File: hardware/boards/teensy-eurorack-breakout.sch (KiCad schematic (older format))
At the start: 74 parts, among them J1 Conn_01x08, SW1 Rotary_Encoder_Switch, SW2 Rotary_Encoder_Switch, SW3 Rotary_Encoder_Switch, U2 AD5754BREZ, U3 AD5754BREZ, U5 MCP1700-2502E, U6 AD7606BSTZ, U7 6N138

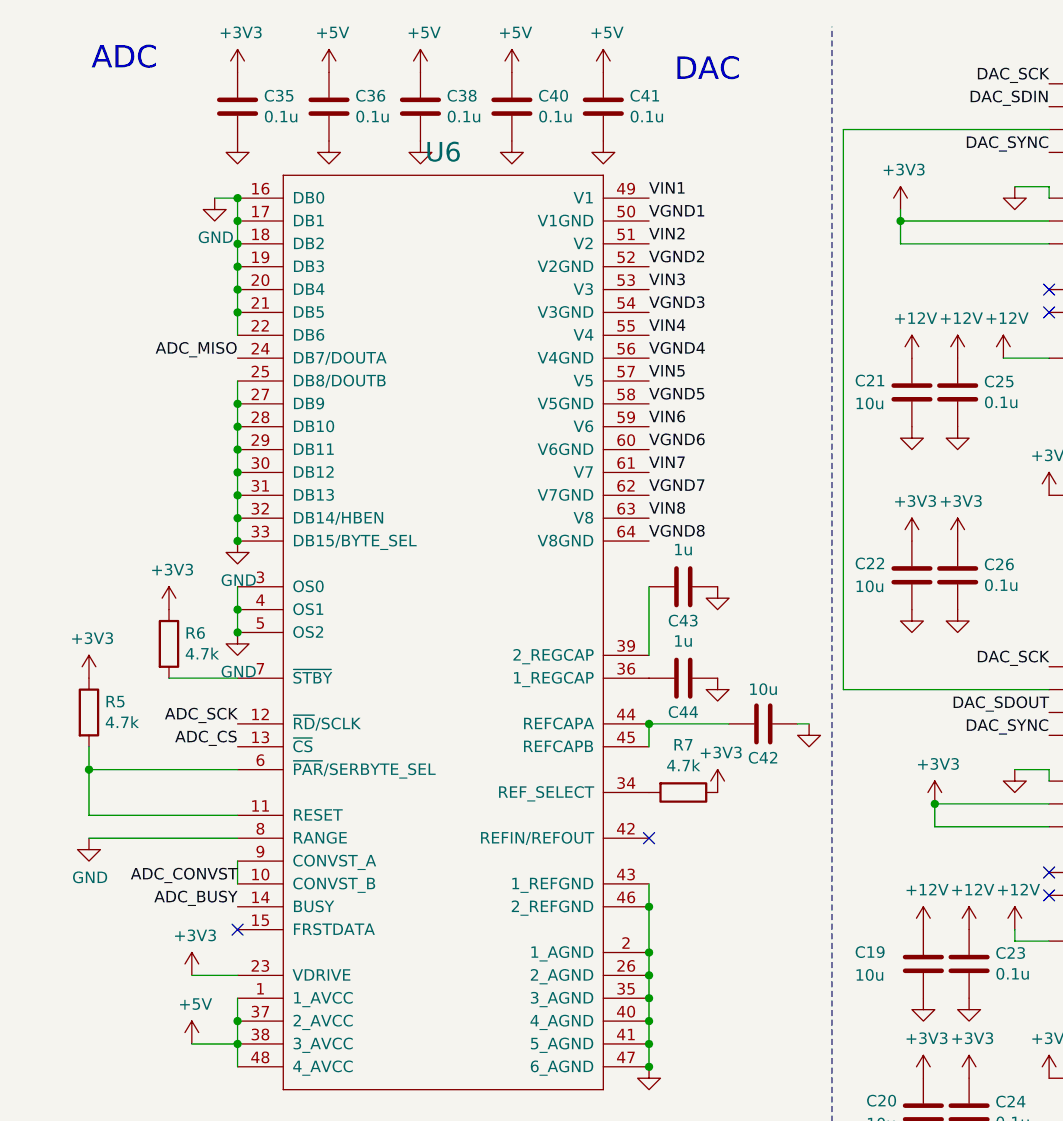
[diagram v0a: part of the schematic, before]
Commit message: fix schematic errors and change breakout to 4 layer board
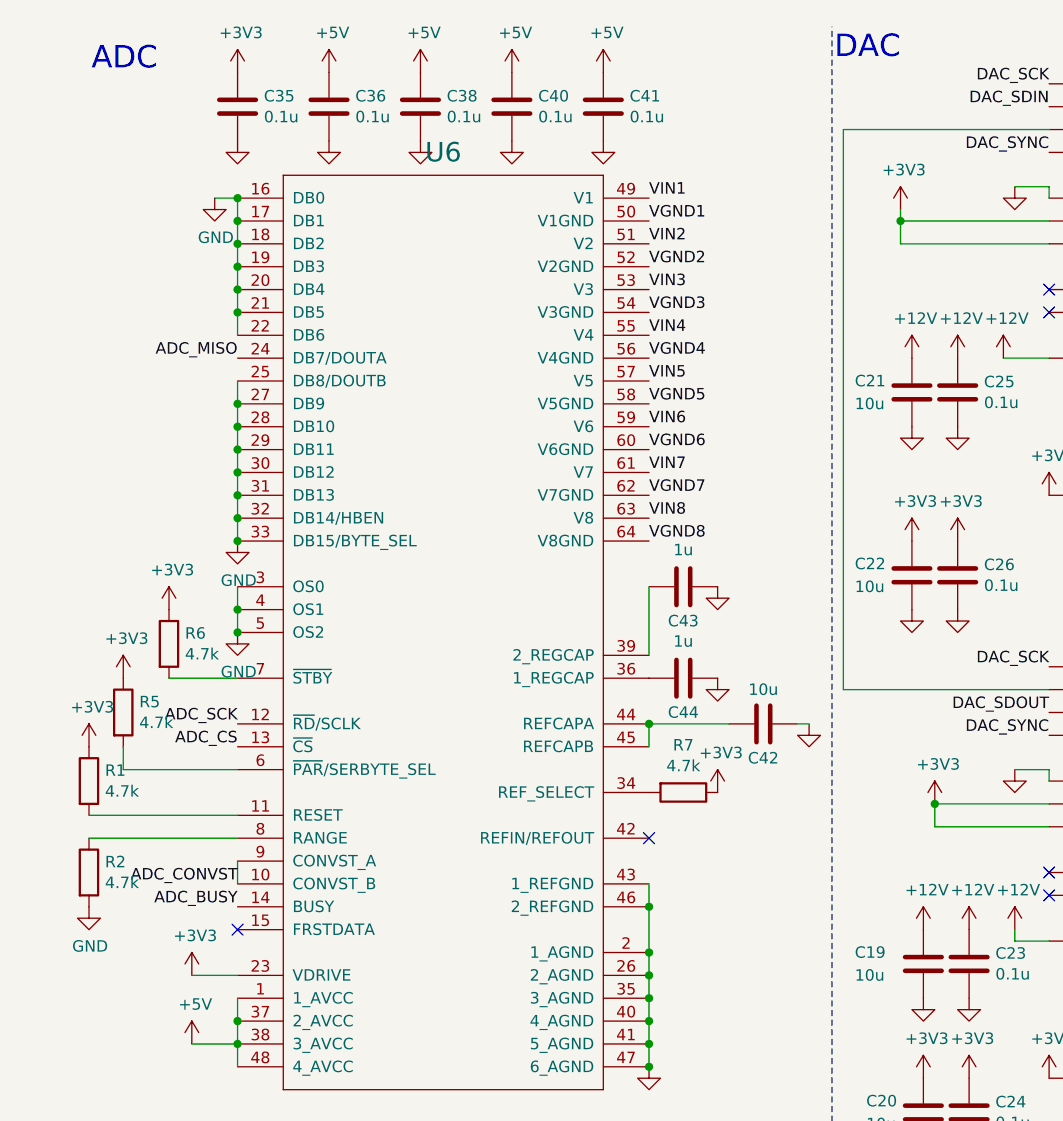
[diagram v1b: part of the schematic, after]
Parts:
- added R1, R2: 4.7k, Resistor_SMD:R_0805_2012Metric, symbol Device:R
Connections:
- net +3V3: now also R1.1
- net GND: now also R2.2; no longer U6.8 (RANGE)
- net at R5.2, U6.6 (~PAR~/SERBYTE_SEL): no longer U6.11 (RESET)
- new net: R1.2, U6.11 (RESET)
- new net: R2.1, U6.8 (RANGE)
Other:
- moved on the sheet: R5
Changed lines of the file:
@@
 L Device:R R5
 U 1 1 5EE69443
-P 550 3500
-F 0 "R5" H 620 3546 50  0000 L CNN
-F 1 "4.7k" H 620 3455 50  0000 L CNN
-F 2 "Resistor_SMD:R_0805_2012Metric" V 480 3500 50  0001 C CNN
-F 3 "~" H 550 3500 50  0001 C CNN
-	1    550  3500
-	1    0    0    -1
-$EndComp
-Wire Wire Line
-	550  3650 550  3750
-Wire Wire Line
-	550  3750 1200 3750
+P 700 3500
+F 0 "R5" H 770 3546 50  0000 L CNN
+F 1 "4.7k" H 770 3455 50  0000 L CNN
+F 2 "Resistor_SMD:R_0805_2012Metric" V 630 3500 50  0001 C CNN
+F 3 "~" H 700 3500 50  0001 C CNN
+	1    700  3500
+	1    0    0    -1
+$EndComp
 $Comp
 L power:+3V3 #PWR073
 U 1 1 5EE6BD54
-P 550 3350
-F 0 "#PWR073" H 550 3200 50  0001 C CNN
-F 1 "+3V3" H 565 3523 50  0000 C CNN
-F 2 "" H 550 3350 50  0001 C CNN
-F 3 "" H 550 3350 50  0001 C CNN
-	1    550  3350
+P 700 3350
+F 0 "#PWR073" H 700 3200 50  0001 C CNN
+F 1 "+3V3" H 715 3523 50  0000 C CNN
+F 2 "" H 700 3350 50  0001 C CNN
+F 3 "" H 700 3350 50  0001 C CNN
+	1    700  3350
 	1    0    0    -1
 $EndComp
@@
 L power:GND #PWR074
 U 1 1 5EE71FB6
-P 550 4050
-F 0 "#PWR074" H 550 3800 50  0001 C CNN
-F 1 "GND" H 555 3877 50  0000 C CNN
-F 2 "" H 550 4050 50  0001 C CNN
-F 3 "" H 550 4050 50  0001 C CNN
-	1    550  4050
+P 550 4350
+F 0 "#PWR074" H 550 4100 50  0001 C CNN
+F 1 "GND" H 555 4177 50  0000 C CNN
+F 2 "" H 550 4350 50  0001 C CNN
+F 3 "" H 550 4350 50  0001 C CNN
+	1    550  4350
 	1    0    0    -1
 $EndComp
@@
 	7950 9550 8000 9550
 Wire Wire Line
-	550  3750 550  3950
-Wire Wire Line
 	550  3950 1200 3950
-Connection ~ 550  3750
 $Comp
 L power:GND #PWR077
@@
 	1    0    0    1
 $EndComp
-Text Notes 3400 750  2    98   ~ 0
+Text Notes 4100 650  2    98   ~ 0
 DAC
 Text Label 6150 3800 0    50   ~ 0
@@
 Wire Notes Line
 	500  5550 7000 5550
+Wire Wire Line
+	700  3650 700  3750
+Wire Wire Line
+	700  3750 1200 3750
+$Comp
+L Device:R R1
+U 1 1 5F517C04
+P 550 3800
+F 0 "R1" H 620 3846 50  0000 L CNN
+F 1 "4.7k" H 620 3755 50  0000 L CNN
+F 2 "Resistor_SMD:R_0805_2012Metric" V 480 3800 50  0001 C CNN
+F 3 "~" H 550 3800 50  0001 C CNN
+	1    550  3800
+	1    0    0    -1
+$EndComp
+$Comp
+L power:+3V3 #PWR01
+U 1 1 5F517C0A
+P 550 3650
+F 0 "#PWR01" H 550 3500 50  0001 C CNN
+F 1 "+3V3" H 565 3823 50  0000 C CNN
+F 2 "" H 550 3650 50  0001 C CNN
+F 3 "" H 550 3650 50  0001 C CNN
+	1    550  3650
+	1    0    0    -1
+$EndComp
+$Comp
+L Device:R R2
+U 1 1 5F5296C2
+P 550 4200
+F 0 "R2" H 620 4246 50  0000 L CNN
+F 1 "4.7k" H 620 4155 50  0000 L CNN
+F 2 "Resistor_SMD:R_0805_2012Metric" V 480 4200 50  0001 C CNN
+F 3 "~" H 550 4200 50  0001 C CNN
+	1    550  4200
+	1    0    0    -1
+$EndComp
 $EndSCHEMATC

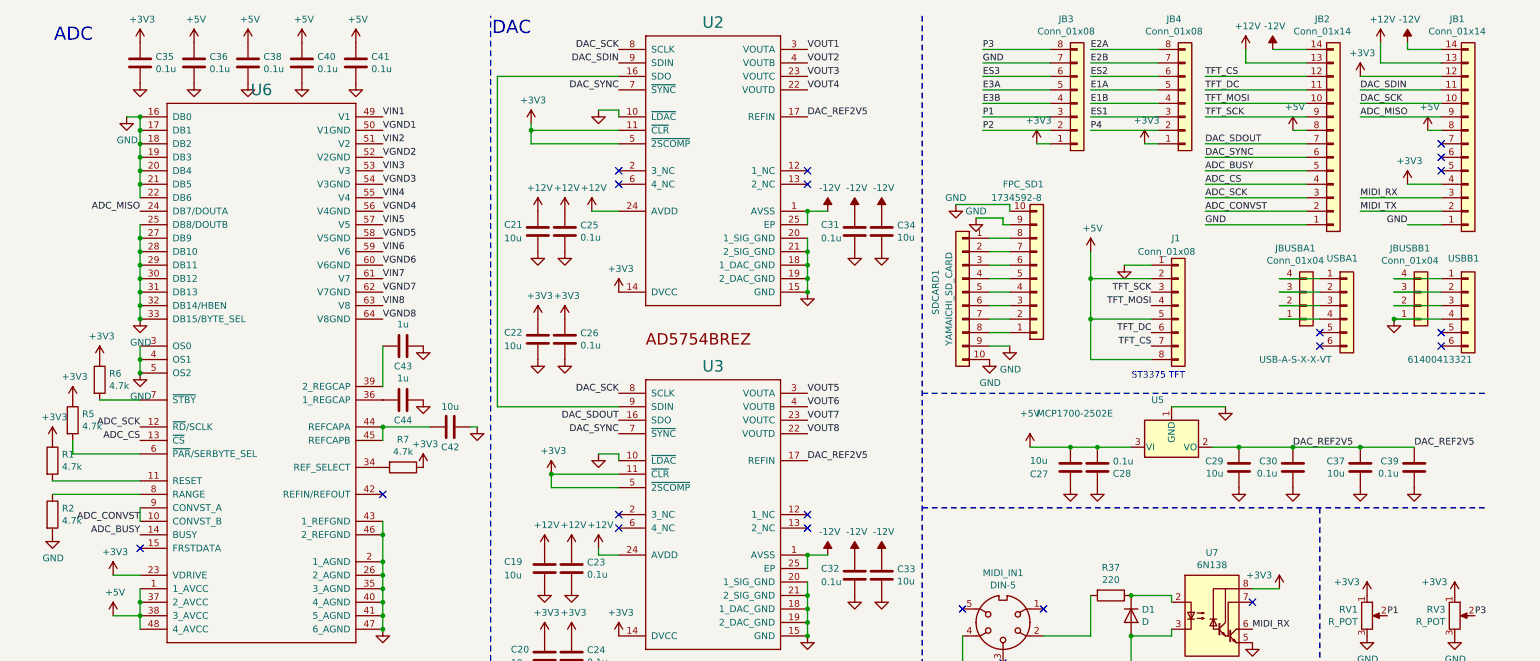
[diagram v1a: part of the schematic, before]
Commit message: schematic: corrections and updates
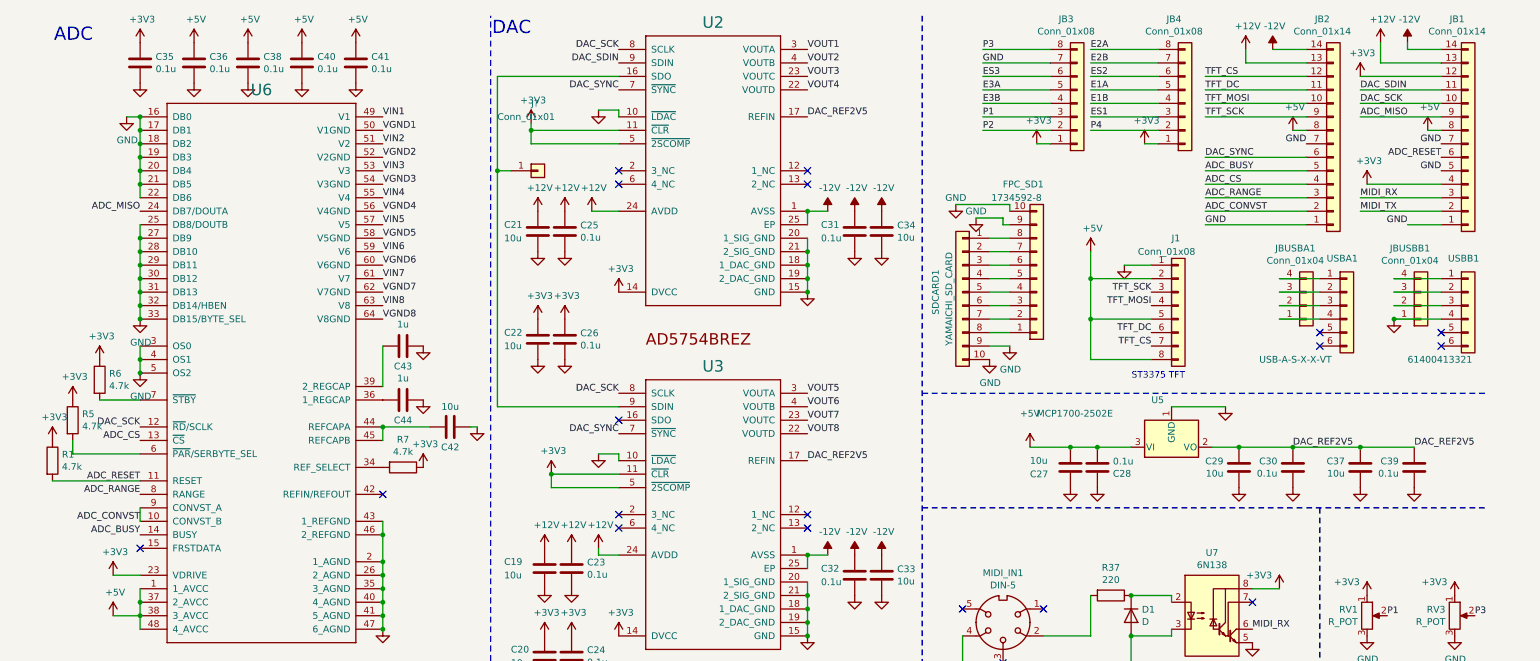
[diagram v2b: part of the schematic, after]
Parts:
- removed R2: 4.7k, Resistor_SMD:R_0805_2012Metric, symbol Device:R
- added J?: Conn_01x01, symbol Connector_Generic:Conn_01x01
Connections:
- net DAC_SCK: now also U6.12 (~RD~/SCLK)
- net GND: now also JB1.5 (Pin_5), JB1.7 (Pin_7), JB2.7 (Pin_7)
- net ADC_RESET: now reaches R1.2, U6.11 (RESET)
- net ADC_RESET: now also JB1.6 (Pin_6)
- net ADC_RANGE: now reaches U6.8 (RANGE)
- net ADC_RANGE: now also JB2.3 (Pin_3)
- net at U2.16 (SDO), U3.9 (SDIN): now also J?.1 (Pin_1)
- removed net ADC_SCK: JB2.3 (Pin_3), U6.12 (~RD~/SCLK)
- net DAC_SDOUT: no longer names the net of U3.16 (SDO)
- net DAC_SDOUT: no longer JB2.7 (Pin_7)
- no-connect marks 32 -> 30
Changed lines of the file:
@@
 Text Label 1200 1950 2    50   ~ 0
 ADC_MISO
-Text Label 1200 3550 2    50   ~ 0
-ADC_SCK
 Text Label 1200 3650 2    50   ~ 0
 ADC_CS
@@
 	1    0    0    -1
 $EndComp
-$Comp
-L power:GND #PWR074
-U 1 1 5EE71FB6
-P 550 4350
-F 0 "#PWR074" H 550 4100 50  0001 C CNN
-F 1 "GND" H 555 4177 50  0000 C CNN
-F 2 "" H 550 4350 50  0001 C CNN
-F 3 "" H 550 4350 50  0001 C CNN
-	1    550  4350
-	1    0    0    -1
-$EndComp
-Wire Wire Line
-	550  4050 1200 4050
 Wire Wire Line
 	1200 4150 1200 4250
@@
 L power:+3V3 #PWR083
 U 1 1 5F063899
-P 10600 1750
-F 0 "#PWR083" H 10600 1600 50  0001 C CNN
-F 1 "+3V3" H 10615 1923 50  0000 C CNN
-F 2 "" H 10600 1750 50  0001 C CNN
-F 3 "" H 10600 1750 50  0001 C CNN
-	1    10600 1750
+P 10300 1750
+F 0 "#PWR083" H 10300 1600 50  0001 C CNN
+F 1 "+3V3" H 10315 1923 50  0000 C CNN
+F 2 "" H 10300 1750 50  0001 C CNN
+F 3 "" H 10300 1750 50  0001 C CNN
+	1    10300 1750
 	1    0    0    -1
 $EndComp
@@
 Text Label 7450 750  0    49   ~ 0
 P3
-$Comp
-L Connector_Generic:Conn_01x14 JB1
-U 1 1 5EF74B39
-P 11050 1450
-F 0 "JB1" H 10968 525 50  0000 C CNN
-F 1 "Conn_01x14" H 10968 616 50  0000 C CNN
-F 2 "Connector_PinSocket_2.54mm:PinSocket_1x14_P2.54mm_Vertical" H 11050 1450 50  0001 C CNN
-F 3 "~" H 11050 1450 50  0001 C CNN
-	1    11050 1450
-	1    0    0    1
-$EndComp
 Wire Wire Line
 	10250 1950 10850 1950
@@
 	-1   0    0    -1
 $EndComp
-NoConn ~ 10850 1450
-NoConn ~ 10850 1550
-NoConn ~ 10850 1650
 NoConn ~ 850  7650
 NoConn ~ 1600 7650
@@
 Wire Wire Line
 	10250 950  10850 950
-Wire Wire Line
-	10600 1750 10850 1750
 Wire Wire Line
 	7850 1450 7950 1450
@@
 	1    0    0    -1
 $EndComp
-Text Label 4750 3500 2    50   ~ 0
-DAC_SDOUT
 NoConn ~ 4750 4300
 NoConn ~ 4750 4200
@@
 	3850 3400 4750 3400
 Wire Wire Line
-	3850 950  3850 3400
+	3850 950  3850 1650
 Wire Wire Line
 	4750 950  3850 950
@@
 	9100 1250 9850 1250
 Wire Wire Line
-	9850 1450 9100 1450
-Wire Wire Line
 	9850 1550 9100 1550
 Text Label 9100 1650 0    49   ~ 0
@@
 ADC_CONVST
 Text Label 9100 1850 0    49   ~ 0
-ADC_SCK
+ADC_RANGE
 Text Label 9100 1750 0    49   ~ 0
 ADC_CS
@@
 Text Label 9100 1550 0    49   ~ 0
 DAC_SYNC
-Text Label 9100 1450 0    49   ~ 0
-DAC_SDOUT
 Wire Wire Line
 	9100 2050 9850 2050
@@
 	1    0    0    -1
 $EndComp
-$Comp
-L Device:R R2
-U 1 1 5F5296C2
-P 550 4200
-F 0 "R2" H 620 4246 50  0000 L CNN
-F 1 "4.7k" H 620 4155 50  0000 L CNN
-F 2 "Resistor_SMD:R_0805_2012Metric" V 480 4200 50  0001 C CNN
-F 3 "~" H 550 4200 50  0001 C CNN
-	1    550  4200
-	1    0    0    -1
-$EndComp
+Text Label 1200 4050 2    49   ~ 0
+ADC_RANGE
+Text Label 1200 3550 2    50   ~ 0
+DAC_SCK
+$Comp
+L Connector_Generic:Conn_01x01 J?
+U 1 1 5FA6E2AB
+P 4150 1650
+F 0 "J?" H 4100 2150 50  0000 L CNN
+F 1 "Conn_01x01" H 3850 2050 50  0000 L CNN
+F 2 "" H 4150 1650 50  0001 C CNN
+F 3 "" H 4150 1650 50  0001 C CNN
+	1    4150 1650
+	1    0    0    -1
+$EndComp
+Wire Wire Line
+	3950 1650 3850 1650
+Connection ~ 3850 1650
+Wire Wire Line
+	3850 1650 3850 3400
+NoConn ~ 4750 3500
+Text Label 9850 1450 2    49   ~ 0
+GND
+$Comp
+L Connector_Generic:Conn_01x14 JB1
+U 1 1 5EF74B39
+P 11050 1450
+F 0 "JB1" H 10968 525 50  0000 C CNN
+F 1 "Conn_01x14" H 10968 616 50  0000 C CNN
+F 2 "Connector_PinSocket_2.54mm:PinSocket_1x14_P2.54mm_Vertical" H 11050 1450 50  0001 C CNN
+F 3 "~" H 11050 1450 50  0001 C CNN
+	1    11050 1450
+	1    0    0    1
+$EndComp
+Text Label 10850 1450 2    49   ~ 0
+GND
+Text Label 10850 1650 2    49   ~ 0
+GND
+Text Label 10850 1550 2    49   ~ 0
+ADC_RESET
+Text Label 1200 3950 2    49   ~ 0
+ADC_RESET
+Wire Wire Line
+	10300 1750 10850 1750
 $EndSCHEMATC

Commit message: schematic, pcb changes for v2.0
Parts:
- removed J?: Conn_01x01, symbol Connector_Generic:Conn_01x01
- C19, C21, C23, C25, C31, C32, C33, C34: footprint Capacitor_SMD:C_0805_2012Metric -> Capacitors_THT:CP_Radial_D5.0mm_P2.00mm
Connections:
- net +12V: now also JB1.14 (Pin_14); no longer JB1.13 (Pin_13), JB2.13 (Pin_13)
- net -12V: now also JB1.13 (Pin_13); no longer JB1.14 (Pin_14), JB2.14 (Pin_14)
- no-connect marks 30 -> 32
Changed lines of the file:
@@
 	10250 1250 10850 1250
-$Comp
-L power:-12V #PWR0150
-U 1 1 5F09F1EE
-P 10600 700
-F 0 "#PWR0150" H 10600 800 50  0001 C CNN
-F 1 "-12V" H 10615 873 50  0000 C CNN
-F 2 "" H 10600 700 50  0001 C CNN
-F 3 "" H 10600 700 50  0001 C CNN
-	1    10600 700
-	1    0    0    -1
-$EndComp
-$Comp
-L power:+12V #PWR0153
-U 1 1 5F0A0CCB
-P 10400 700
-F 0 "#PWR0153" H 10400 550 50  0001 C CNN
-F 1 "+12V" H 10415 873 50  0000 C CNN
-F 2 "" H 10400 700 50  0001 C CNN
-F 3 "" H 10400 700 50  0001 C CNN
-	1    10400 700
-	1    0    0    -1
-$EndComp
-Wire Wire Line
-	10600 700  10600 750
-Wire Wire Line
-	10600 750  10850 750
-Wire Wire Line
-	10400 700  10400 850
-Wire Wire Line
-	10400 850  10850 850
 $Comp
 L power:+5V #PWR0154
@@
 F 0 "C33" H 6815 4696 50  0000 L CNN
 F 1 "10u" H 6815 4605 50  0000 L CNN
-F 2 "Capacitor_SMD:C_0805_2012Metric" H 6738 4500 50  0001 C CNN
+F 2 "Capacitors_THT:CP_Radial_D5.0mm_P2.00mm" H 6738 4500 50  0001 C CNN
 F 3 "~" H 6700 4650 50  0001 C CNN
 	1    6700 4650
@@
 F 0 "C32" H 6250 4700 50  0000 L CNN
 F 1 "0.1u" H 6250 4600 50  0000 L CNN
-F 2 "Capacitor_SMD:C_0805_2012Metric" H 6538 4500 50  0001 C CNN
+F 2 "Capacitors_THT:CP_Radial_D5.0mm_P2.00mm" H 6538 4500 50  0001 C CNN
 F 3 "~" H 6500 4650 50  0001 C CNN
 	1    6500 4650
@@
 F 0 "C23" H 4515 4646 50  0000 L CNN
 F 1 "0.1u" H 4515 4555 50  0000 L CNN
-F 2 "Capacitor_SMD:C_0805_2012Metric" H 4438 4450 50  0001 C CNN
+F 2 "Capacitors_THT:CP_Radial_D5.0mm_P2.00mm" H 4438 4450 50  0001 C CNN
 F 3 "~" H 4400 4600 50  0001 C CNN
 	1    4400 4600
@@
 F 0 "C19" H 3900 4650 50  0000 L CNN
 F 1 "10u" H 3900 4550 50  0000 L CNN
-F 2 "Capacitor_SMD:C_0805_2012Metric" H 4238 4450 50  0001 C CNN
+F 2 "Capacitors_THT:CP_Radial_D5.0mm_P2.00mm" H 4238 4450 50  0001 C CNN
 F 3 "~" H 4200 4600 50  0001 C CNN
 	1    4200 4600
@@
 F 0 "C34" H 6815 2146 50  0000 L CNN
 F 1 "10u" H 6815 2055 50  0000 L CNN
-F 2 "Capacitor_SMD:C_0805_2012Metric" H 6738 1950 50  0001 C CNN
+F 2 "Capacitors_THT:CP_Radial_D5.0mm_P2.00mm" H 6738 1950 50  0001 C CNN
 F 3 "~" H 6700 2100 50  0001 C CNN
 	1    6700 2100
@@
 F 0 "C21" H 3900 2150 50  0000 L CNN
 F 1 "10u" H 3900 2050 50  0000 L CNN
-F 2 "Capacitor_SMD:C_0805_2012Metric" H 4188 1950 50  0001 C CNN
+F 2 "Capacitors_THT:CP_Radial_D5.0mm_P2.00mm" H 4188 1950 50  0001 C CNN
 F 3 "~" H 4150 2100 50  0001 C CNN
 	1    4150 2100
@@
 F 0 "C31" H 6250 2150 50  0000 L CNN
 F 1 "0.1u" H 6250 2050 50  0000 L CNN
-F 2 "Capacitor_SMD:C_0805_2012Metric" H 6538 1950 50  0001 C CNN
+F 2 "Capacitors_THT:CP_Radial_D5.0mm_P2.00mm" H 6538 1950 50  0001 C CNN
 F 3 "~" H 6500 2100 50  0001 C CNN
 	1    6500 2100
-	1    0    0    -1
-$EndComp
-$Comp
-L Device:C C25
-U 1 1 5EFEB20A
-P 4350 2100
-F 0 "C25" H 4465 2146 50  0000 L CNN
-F 1 "0.1u" H 4465 2055 50  0000 L CNN
-F 2 "Capacitor_SMD:C_0805_2012Metric" H 4388 1950 50  0001 C CNN
-F 3 "~" H 4350 2100 50  0001 C CNN
-	1    4350 2100
 	1    0    0    -1
 $EndComp
@@
 	3850 3400 4750 3400
 Wire Wire Line
-	3850 950  3850 1650
-Wire Wire Line
 	4750 950  3850 950
 $Comp
@@
 	1    0    0    -1
 $EndComp
-Wire Wire Line
-	9600 750  9850 750
 Text Label 9100 1050 0    49   ~ 0
 TFT_DC
@@
 Wire Wire Line
 	9100 1150 9850 1150
-$Comp
-L power:-12V #PWR0151
-U 1 1 5F09FD24
-P 9600 750
-F 0 "#PWR0151" H 9600 850 50  0001 C CNN
-F 1 "-12V" H 9615 923 50  0000 C CNN
-F 2 "" H 9600 750 50  0001 C CNN
-F 3 "" H 9600 750 50  0001 C CNN
-	1    9600 750
-	1    0    0    -1
-$EndComp
-$Comp
-L power:+12V #PWR0152
-U 1 1 5F0A0203
-P 9400 750
-F 0 "#PWR0152" H 9400 600 50  0001 C CNN
-F 1 "+12V" H 9415 923 50  0000 C CNN
-F 2 "" H 9400 750 50  0001 C CNN
-F 3 "" H 9400 750 50  0001 C CNN
-	1    9400 750
-	1    0    0    -1
-$EndComp
-Wire Wire Line
-	9400 750  9400 850
-Wire Wire Line
-	9400 850  9850 850
 Text Label 9100 1550 0    49   ~ 0
 DAC_SYNC
@@
 Text Label 1200 3550 2    50   ~ 0
 DAC_SCK
-$Comp
-L Connector_Generic:Conn_01x01 J?
-U 1 1 5FA6E2AB
-P 4150 1650
-F 0 "J?" H 4100 2150 50  0000 L CNN
-F 1 "Conn_01x01" H 3850 2050 50  0000 L CNN
-F 2 "" H 4150 1650 50  0001 C CNN
-F 3 "" H 4150 1650 50  0001 C CNN
-	1    4150 1650
-	1    0    0    -1
-$EndComp
-Wire Wire Line
-	3950 1650 3850 1650
-Connection ~ 3850 1650
-Wire Wire Line
-	3850 1650 3850 3400
 NoConn ~ 4750 3500
 Text Label 9850 1450 2    49   ~ 0
@@
 Wire Wire Line
 	10300 1750 10850 1750
+Wire Wire Line
+	10600 750  10850 750
+Wire Wire Line
+	10600 700  10600 750
+$Comp
+L power:-12V #PWR0150
+U 1 1 5F09F1EE
+P 10400 700
+F 0 "#PWR0150" H 10400 800 50  0001 C CNN
+F 1 "-12V" H 10415 873 50  0000 C CNN
+F 2 "" H 10400 700 50  0001 C CNN
+F 3 "" H 10400 700 50  0001 C CNN
+	1    10400 700
+	1    0    0    -1
+$EndComp
+Wire Wire Line
+	10400 700  10400 850
+$Comp
+L power:+12V #PWR0153
+U 1 1 5F0A0CCB
+P 10600 700
+F 0 "#PWR0153" H 10600 550 50  0001 C CNN
+F 1 "+12V" H 10615 873 50  0000 C CNN
+F 2 "" H 10600 700 50  0001 C CNN
+F 3 "" H 10600 700 50  0001 C CNN
+	1    10600 700
+	1    0    0    -1
+$EndComp
+Wire Wire Line
+	10400 850  10850 850
+NoConn ~ 9850 850
+NoConn ~ 9850 750
+$Comp
+L Device:C C25
+U 1 1 5EFEB20A
+P 4350 2100
+F 0 "C25" H 4465 2146 50  0000 L CNN
+F 1 "0.1u" H 4465 2055 50  0000 L CNN
+F 2 "Capacitors_THT:CP_Radial_D5.0mm_P2.00mm" H 4388 1950 50  0001 C CNN
+F 3 "~" H 4350 2100 50  0001 C CNN
+	1    4350 2100
+	1    0    0    -1
+$EndComp
+Wire Wire Line
+	3850 950  3850 3400
 $EndSCHEMATC
